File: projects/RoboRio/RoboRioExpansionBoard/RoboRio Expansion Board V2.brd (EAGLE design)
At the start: 56.6 x 77.5 mm, 133 parts, among them J1 RRINTERFACE-FEMALE, J10 SPI_MISO, J11 SPI_MOSI, J12 I2C_SCL, J13 I2C_SDA, J14 UART_TX, J15 UART_RX, J16 LCD, J17 ADC1, J18 ADC2, J19 ADC3, J2 MICROSD-HINGED, J20 ADC4, J21 ADC5, J22 ADC6, J23 ADC7, J25 PWM0, J26 PWM1, J27 PWM2, J28 PWM3, J29 PWM4, J3 51387-0578, J30 PWM5, J31 PWM6, J32 PWM7, J33 PWM8, J34 PWM9, J35 AI0, J36 AI1, J37 AI2, J38 AI3, J39 AO0, J4 GPIO0, J40 AO1, J5 GPIO1, J6 GPIO2, J7 GPIO3, J8 SPI_CS, J9 SPI_CLK, Q1 NPN-SOT416, Q2 NPN-SOT416, Q3 NPN-SOT416, SW1 450-1781-ND, U1 FTS31XS-U, U2 24LC256ST, U3 REG1117, U4 TPS2115APWR, U5 P8X32A-Q44_P, U6 TC54VN43, U7 ADC124S01, U8 ADC124S01, Y1 5MHz

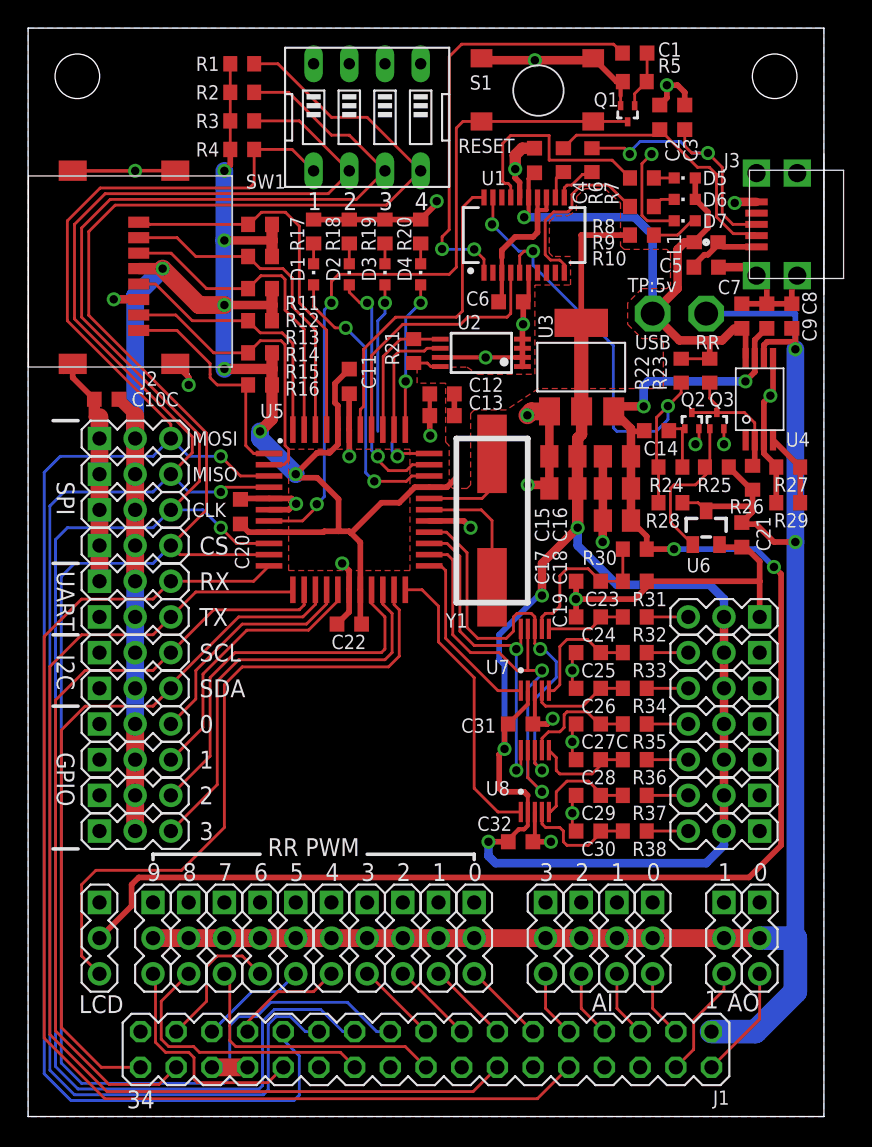
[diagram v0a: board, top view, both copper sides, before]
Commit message: silk updates, 5VRR changes
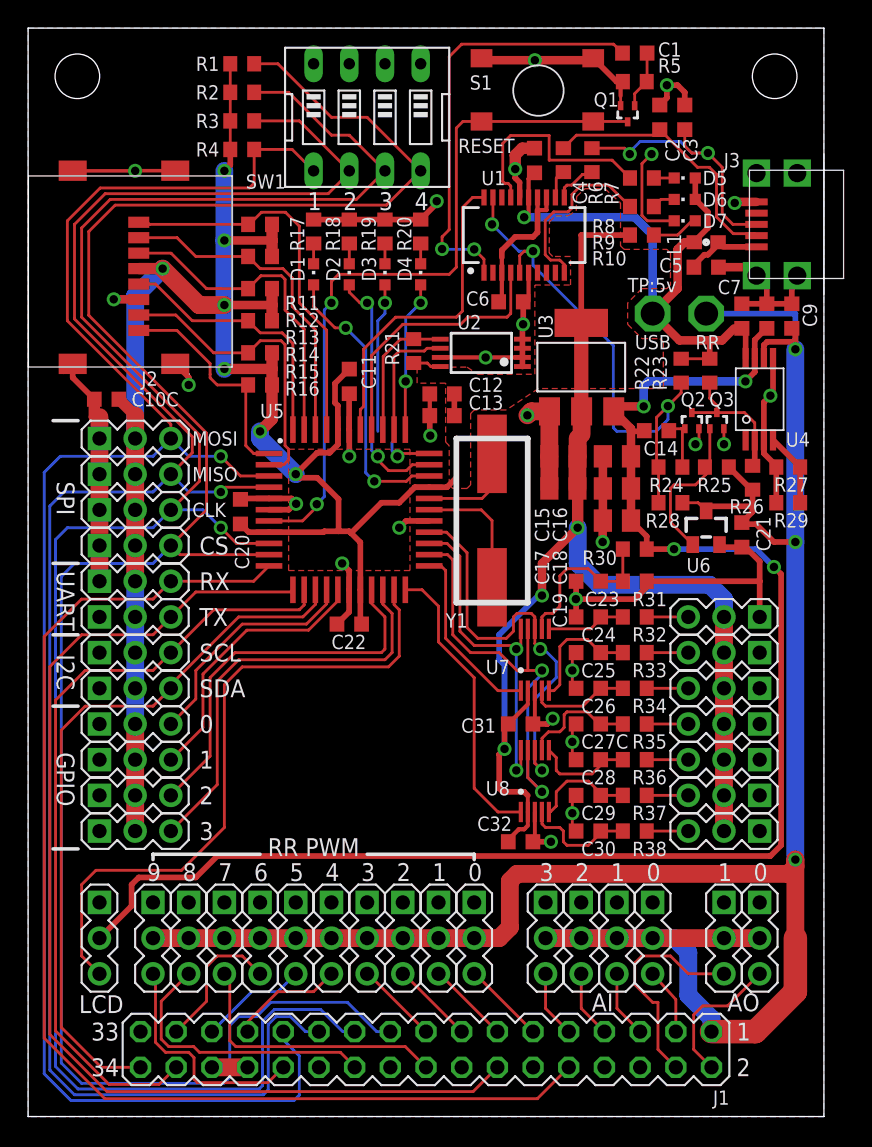
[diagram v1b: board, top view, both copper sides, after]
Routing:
- net 5VRR: track 127.1 -> 163.8 mm, vias 2 -> 3
- net +3V3: track 249.9 -> 229.7 mm, vias 11 -> 10
- net AO1: track 8.08 -> 15.9 mm
- net DGND: track 187.0 -> 184.6 mm, vias 28 -> 27
- net AO0: track 8.08 -> 10.2 mm

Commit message: AGND and 5VRR power changes
Cut DGND plane.  Do not join at pin 6 of RR connector.  Split power
between analog and digital from pin 2.
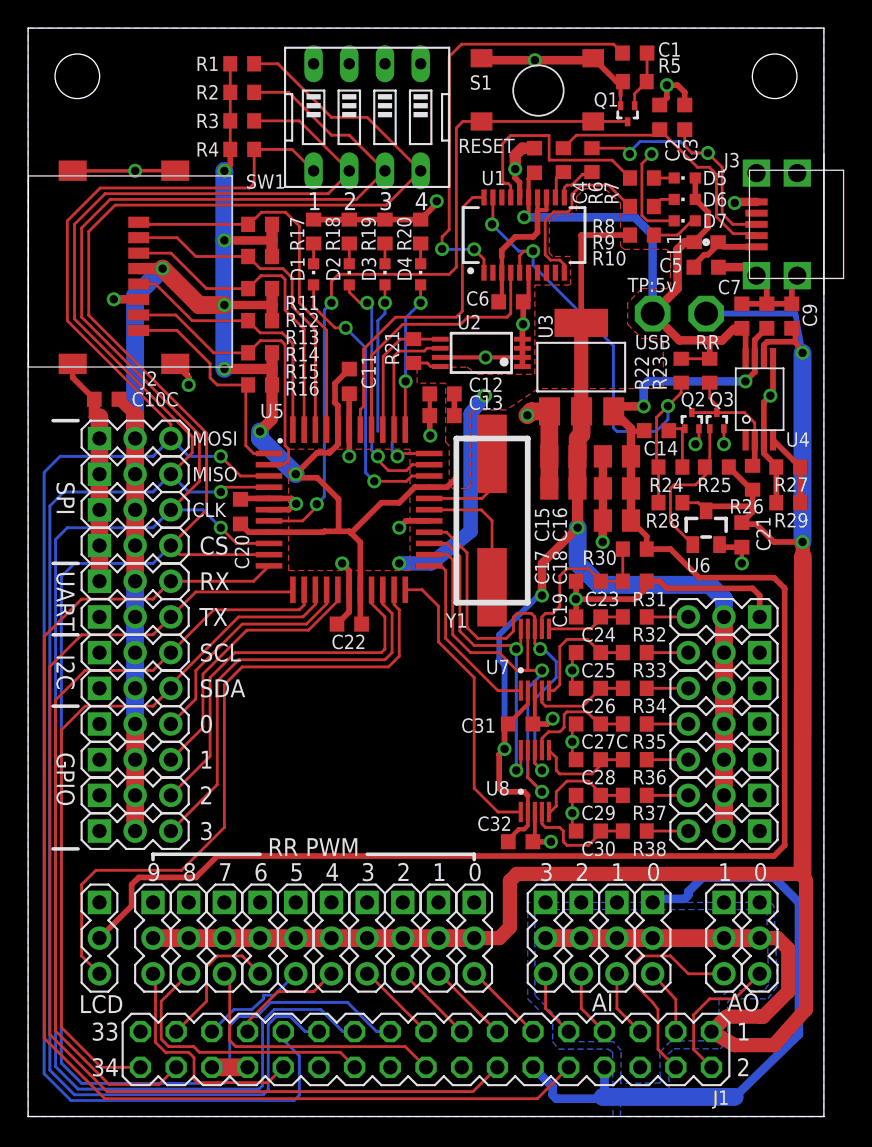
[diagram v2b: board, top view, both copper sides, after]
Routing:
- net DGND: track 184.6 -> 228.2 mm, vias 27 -> 28
- net 5VRR: track 163.8 -> 186.9 mm, vias 3 -> 2
- net +3V3: track 229.7 -> 245.6 mm, vias 10 -> 12
- net +5V: track 109.0 -> 108.9 mm, vias 4 -> 2

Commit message: Run DRC and remove errors
22 approved errors left.  I don't know whey it went down so far from
235.  Still need to add silk for power on 3-pin connectors (which of the
3 pins are power gnd and signal)
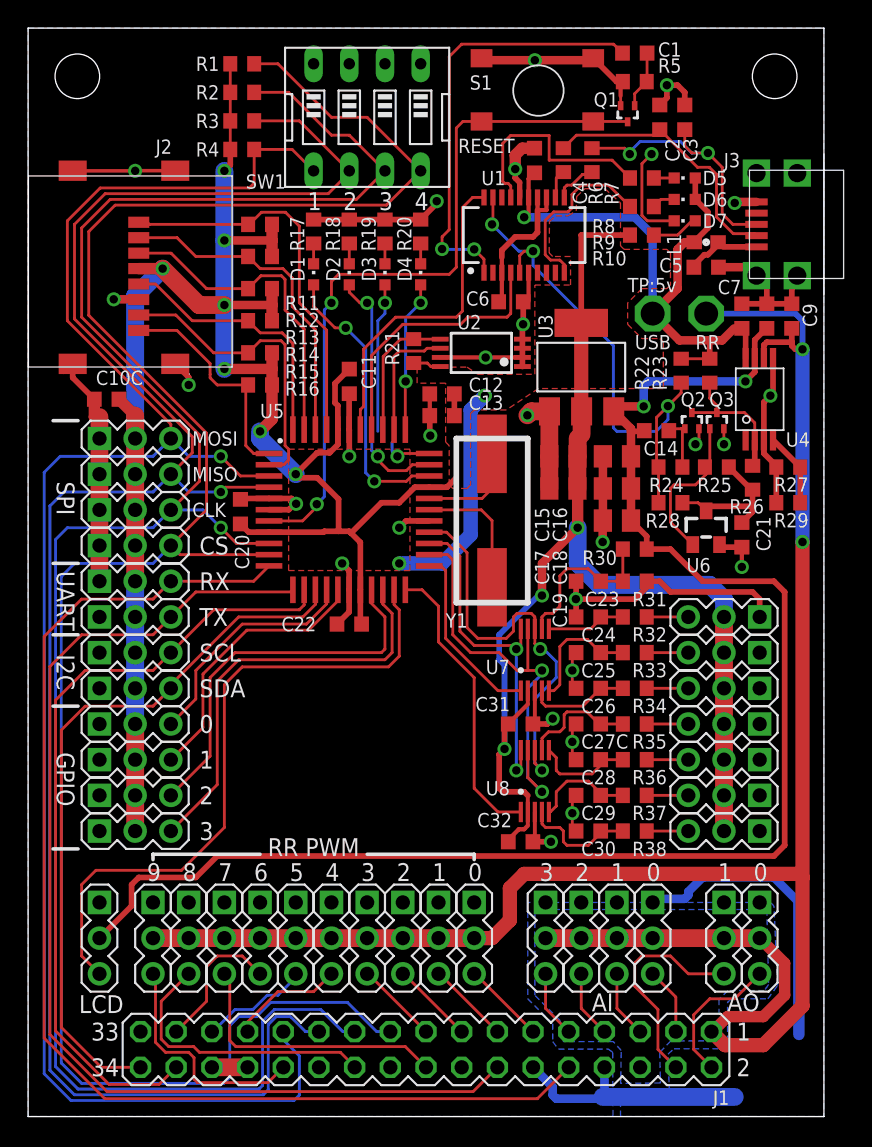
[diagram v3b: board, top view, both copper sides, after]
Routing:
- net 5VRR: track 186.9 -> 155.3 mm
- net DGND: track 228.2 -> 222.0 mm

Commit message: Added Fiducials
Also fixed a small silk error
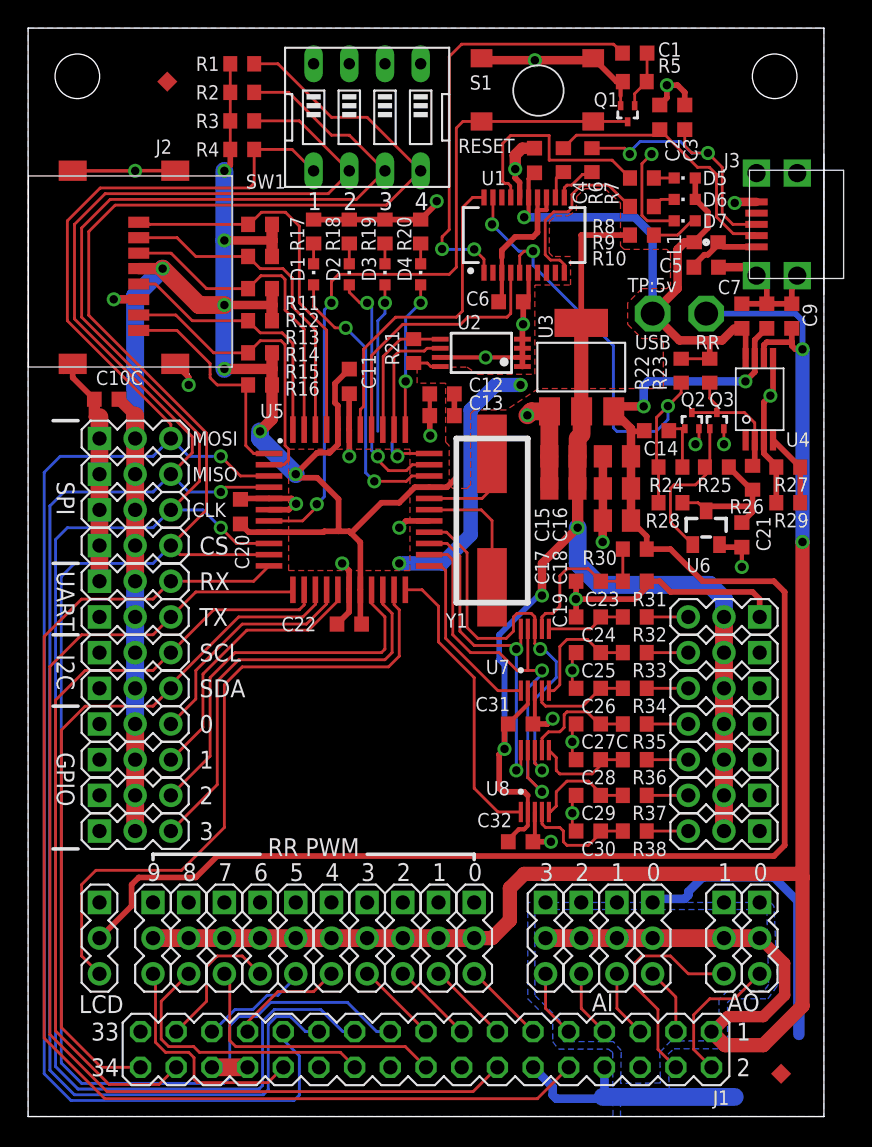
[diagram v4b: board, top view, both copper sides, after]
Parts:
- added U$1, U$2: FIDUCIAL_DIAMOND, fiducial:FIDUCIAL_40MIL_DIAMOND
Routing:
- net +3V3: track 246.0 -> 248.8 mm

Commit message: Silk updates, route air wires
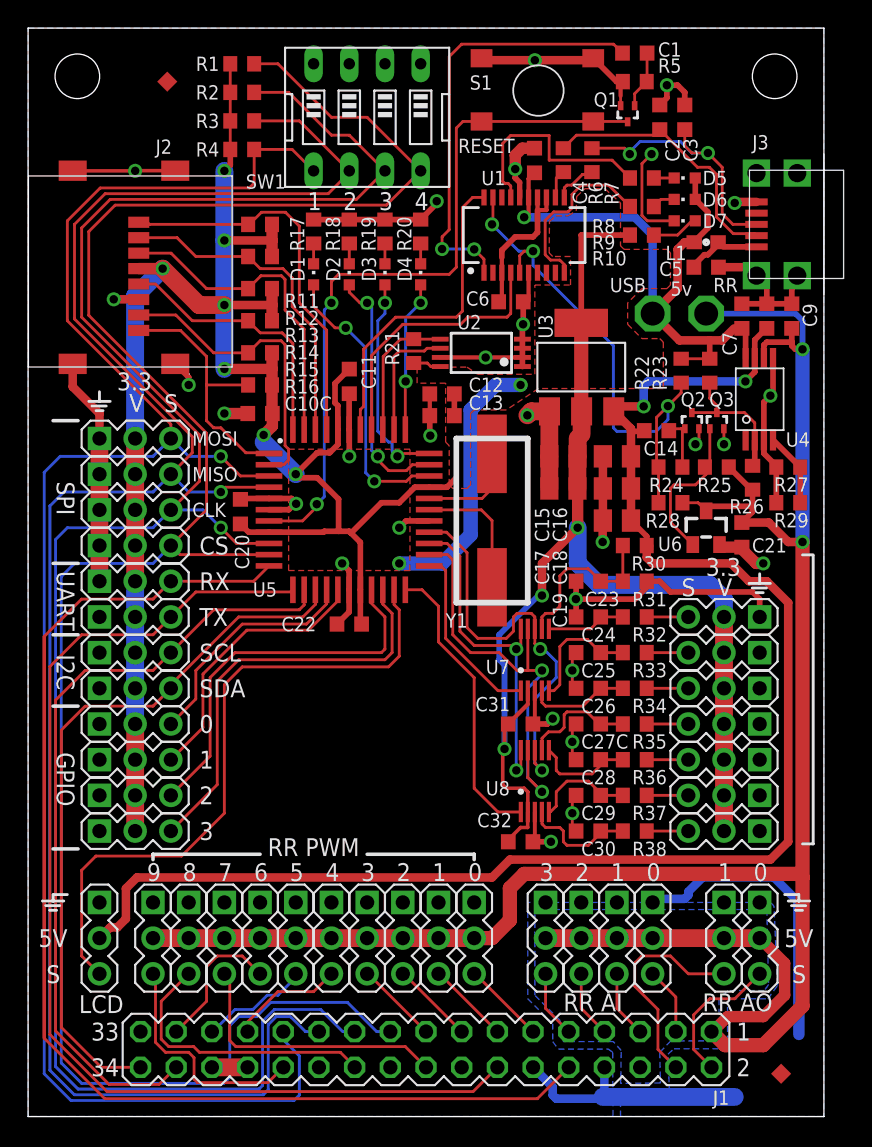
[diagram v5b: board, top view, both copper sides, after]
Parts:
- moved C10C 11.0 mm to (16.5, 50.0)
- moved R30 0.25 mm to (43.2, 40.6)
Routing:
- net IO10: track 86.7 -> 115.3 mm
- net 5VRR: track 155.3 -> 160.2 mm
- net DGND: track 222.0 -> 225.1 mm, vias 28 -> 29
- net IO4: track 16.3 -> 18.7 mm
- net +3V3: track 248.8 -> 247.2 mm
- net IO26: track 14.2 -> 15.5 mm
- net +5V: track 108.8 -> 109.9 mm
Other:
- board text added: "3.3"
- board text added: "5V"
- board text added: "5v"
- board text added: "ADC"
- board text added: "RR AI"
- board text added: "RR AO"
- board text added: "S"
- board text added: "V"
- board text removed: "ADC:"
- board text removed: "AI"
- board text removed: "AO"
- board text removed: "TP:5v"

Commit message: add buffer, re-sequence ref-designators
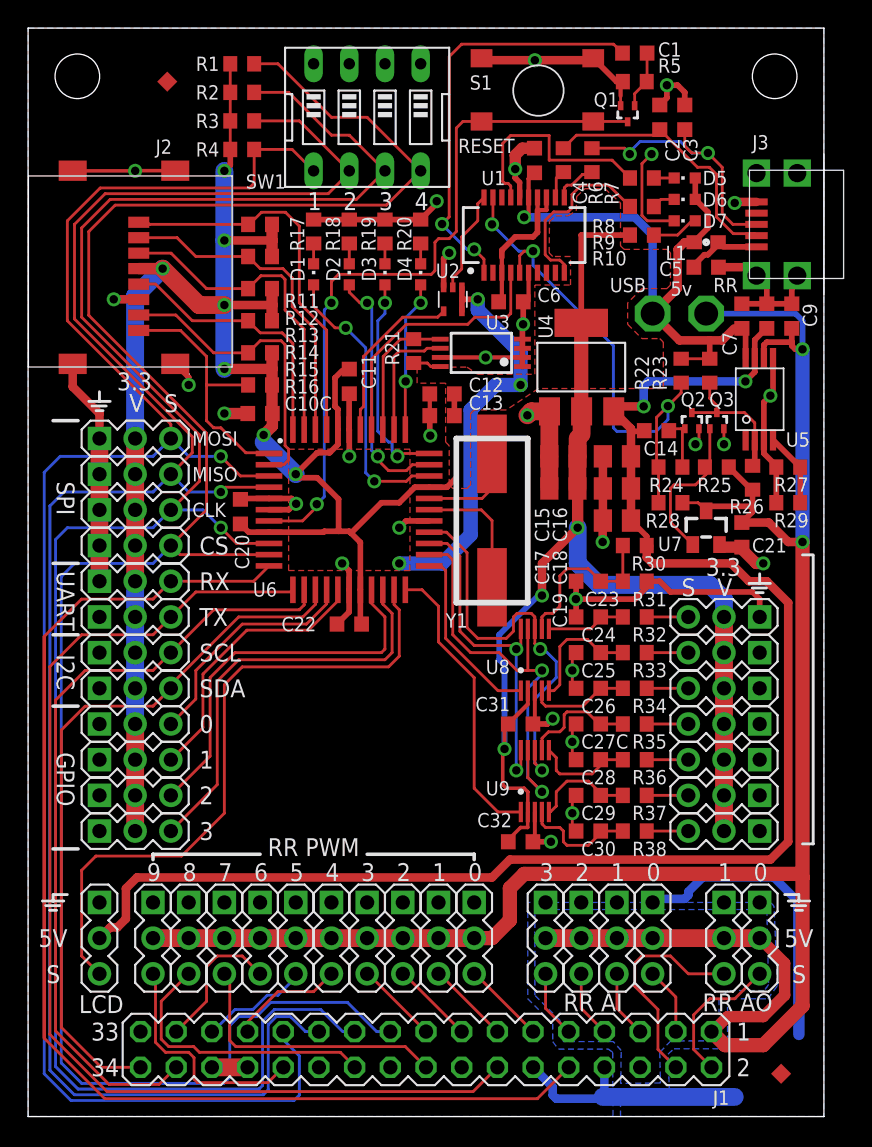
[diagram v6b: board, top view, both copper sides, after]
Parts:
- added U9: ADC124S01, adc124s021cimm:ADC124S021VSSOP
- U2: value 24LC256ST -> 74LVC1G126DCK; device microchip:TSSOP8 -> 74xx-little-us:SC70-5
- U3: value REG1117 -> 24LC256ST; device burr-brown:SOT223 -> microchip:TSSOP8
- U4: value TPS2115APWR -> REG1117; device tps2115apwr:TSSOP-8 -> burr-brown:SOT223
- U5: value P8X32A-Q44_P -> TPS2115APWR; device parallax_propeller:P8X32A-Q44 -> tps2115apwr:TSSOP-8
- U6: value TC54VN43 -> P8X32A-Q44_P; device m-pad-2.1:SOT23 -> parallax_propeller:P8X32A-Q44
- U7: value ADC124S01 -> TC54VN43; device adc124s021cimm:ADC124S021VSSOP -> m-pad-2.1:SOT23
- moved U5 30.3 mm to (52.1, 51.1), turned to 90 degrees
- moved U6 25.4 mm to (22.9, 43.2)
- moved U7 15.4 mm to (48.3, 41.9)
- moved U4 12.9 mm to (39.4, 53.3), turned to 0 degrees
- moved U8 8.64 mm to (36.1, 32.5)
- moved U3 7.18 mm to (32.3, 54.4), turned to 90 degrees
- moved U2 4.32 mm to (30.2, 58.2), turned to 180 degrees
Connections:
- new net USB_TX: U1.20, U2.2
- net !RESET: now also U6.7; no longer U5.7
- net +3V3: now also U2.1, U2.5, U3.8, U4.2, U4.4, U6.18, U6.30, U6.40, U6.8, U9.P$2; no longer U2.8, U3.2, U3.4, U5.18, U5.30, U5.40, U5.8, U7.P$2
- net +5V: now also U4.3, U5.P$7; no longer U3.3, U4.P$7
- net 5VRR: now also U5.P$6, U7.3; no longer U4.P$6, U6.3
- net 5VUSB: now also U5.P$8; no longer U4.P$8
- net DGND: now also U3.2, U3.3, U3.4, U3.7, U4.1, U5.P$3, U5.P$5, U6.17, U6.27, U6.39, U6.5, U6.6, U7.2, U9.P$3; no longer U2.1, U2.2, U2.4, U2.7, U4.P$3, U4.P$5, U5.17, U5.27, U5.39, U5.5, U5.6, U6.2, U7.P$3
- net IO0: now also U6.41; no longer U5.41
- net IO1: now also U6.42; no longer U5.42
- net IO10: now also U6.11; no longer U5.11
- net IO11: now also U6.12; no longer U5.12
- net IO12: now also U6.13; no longer U5.13
- net IO13: now also U6.14; no longer U5.14
- net IO14: now also U6.15; no longer U5.15
- net IO15: now also U6.16; no longer U5.16
- net IO16: now also U6.19; no longer U5.19
- net IO17: now also U6.20; no longer U5.20
- net IO18: now also U6.21; no longer U5.21
- net IO19: now also U6.22, U9.P$1; no longer U5.22, U8.P$1
- net IO2: now also U6.43; no longer U5.43
- net IO20: now also U6.23, U8.P$1; no longer U5.23, U7.P$1
- net IO21: now also U6.24, U9.P$9; no longer U5.24, U7.P$9
- net IO22: now also U6.25, U9.P$10; no longer U5.25, U7.P$10
- net IO23: now also U6.26, U9.P$8; no longer U5.26, U7.P$8
- net IO24: now also U6.31; no longer U5.31
- net IO25: now also U6.32; no longer U5.32
- net IO26: now also U6.33; no longer U5.33
- net IO27: now also U6.34; no longer U5.34
- net IO28_SCL: now also U3.6, U6.35; no longer U2.6, U5.35
- net IO29_SDA: now also U3.5, U6.36; no longer U2.5, U5.36
- net IO3: now also U6.44; no longer U5.44
- net IO30_TX: now also U6.37; no longer U5.37
- net IO31_RX: now also U2.4, U6.38; no longer U1.20, U5.38
- net IO4: now also U6.1; no longer U5.1
- net IO5: now also U6.2; no longer U5.2
- net IO6: now also U6.3; no longer U5.3
- net IO7: now also U6.4; no longer U5.4
- net IO8: now also U6.9; no longer U5.9
- net IO9: now also U6.10; no longer U5.10
- net N$10: now also U9.P$4; no longer U8.P$4
- net N$11: now also U5.P$4; no longer U4.P$4
- net N$15: now also U8.P$4; no longer U7.P$4
- net N$16: now also U8.P$6; no longer U7.P$6
- net N$20: now also U5.P$2; no longer U4.P$2
- net N$21: now also U8.P$5; no longer U7.P$5
- net N$25: now also U8.P$7; no longer U7.P$7
- net N$30: now also U9.P$5; no longer U8.P$5
- net N$32: now also U6.29; no longer U5.29
- net N$37: now also U6.28; no longer U5.28
- net N$38: now also U9.P$6; no longer U8.P$6
- net N$41: now also U9.P$7; no longer U8.P$7
- net RR_PWR_OK: now also U7.1; no longer U6.1
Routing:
- net IO31_RX: track 23.2 -> 12.3 mm
- net +3V3: track 247.2 -> 257.6 mm, vias 12 -> 13
- net USB_TX: track 0.00 -> 7.32 mm
- net DGND: track 225.1 -> 227.8 mm, vias 29 -> 30
- net N$19: track 31.1 -> 30.1 mm
